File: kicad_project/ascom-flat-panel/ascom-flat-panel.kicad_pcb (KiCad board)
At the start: 2 copper layers, 12 parts, among them J1 Servo, J3 JST-XH LED, Q1 FQP30N06L, Q2 FQP30N06L, U1 XIAO-SAMD21-DIP

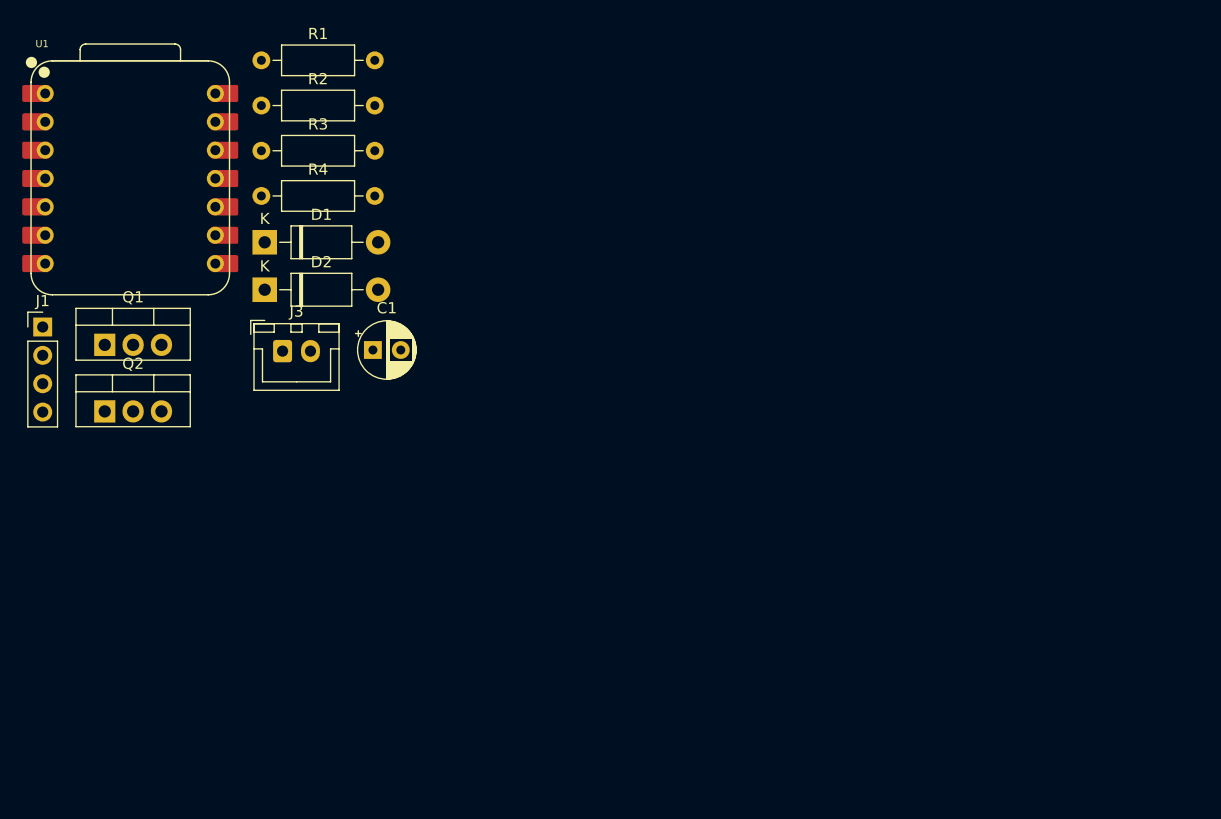
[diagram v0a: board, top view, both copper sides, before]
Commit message: Première mise en forme et routage du circuit - ajout modèle3D seeeduino
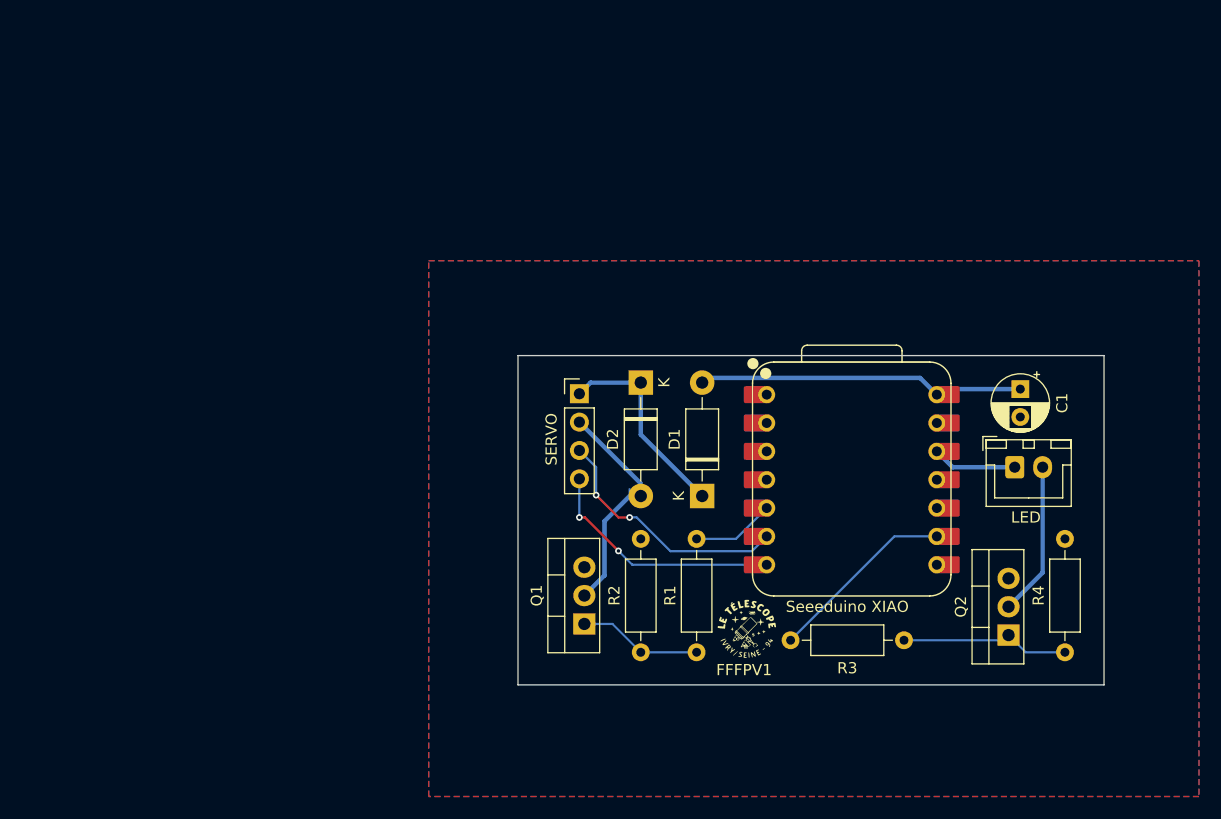
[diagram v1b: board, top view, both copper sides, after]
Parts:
- added G***: LOGO, LOGO, F.Cu at (118.5, 94.0)
- Seeeduino XIAO: renamed from U1
- moved Q2 83.4 mm to (141.9, 94.5), turned to 90 degrees
- moved R4 82.8 mm to (147.0, 96.1), turned to 90 degrees
- moved Seeeduino XIAO 70.0 mm to (128.0, 80.6)
- moved LED 66.4 mm to (142.5, 79.5)
- moved R1 65.8 mm to (114.0, 96.1), turned to 90 degrees
- moved R3 64.6 mm to (122.4, 95.0)
- moved R2 59.6 mm to (109.0, 96.1), turned to 90 degrees
- moved C1 58.1 mm to (143.0, 72.5), turned to -90 degrees
- moved Q1 49.7 mm to (103.9, 93.5), turned to 90 degrees
- moved SERVO 48.5 mm to (103.5, 72.9)
- moved D1 45.3 mm to (114.5, 82.1), turned to 90 degrees
- moved D2 34.7 mm to (109.0, 71.9), turned to -90 degrees
- renumbered J3 to LED, J1 to SERVO
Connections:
- Seeeduino XIAO pad 10: SERVO POSITION CONTROL -> unconnected-(U1-PA5_A9_D9_MISO-Pad10)
- Seeeduino XIAO pad 5: unconnected-(U1-PA8_A4_D4_SDA-Pad5) -> SERVO POWER CONTROL
- Seeeduino XIAO pad 6: unconnected-(U1-PA9_A5_D5_SCL-Pad6) -> SERVO POSITION CONTROL
- Seeeduino XIAO pad 8: SERVO POWER CONTROL -> unconnected-(U1-PB09_A7_D7_RX-Pad8)
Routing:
- net +5V: track 0.00 -> 29.5 mm
- net SERVO POSITION CONTROL: track 0.00 -> 22.5 mm, vias 0 -> 2
- net SERVO POSITION FEEDBACK: track 0.00 -> 22.0 mm, vias 0 -> 2
- net SERVO GND: track 0.00 -> 20.1 mm
- net SERVO VCC: track 0.00 -> 18.4 mm
- net LED_STRIP_POWER_CONTROL: track 0.00 -> 17.0 mm
- net Net-(Q2-G): track 0.00 -> 15.8 mm
- net Net-(J3-Pin_2): track 0.00 -> 13.8 mm
- net Net-(Q1-G): track 0.00 -> 11.1 mm
- net +3V3: track 0.00 -> 7.57 mm
- net SERVO POWER CONTROL: track 0.00 -> 7.42 mm
- added copper zone on B.Cu, net GND
- added copper zone on F.Cu, net GND
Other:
- board outline added: 52.5 x 29.5 mm
- board text added: "FFFPV1"

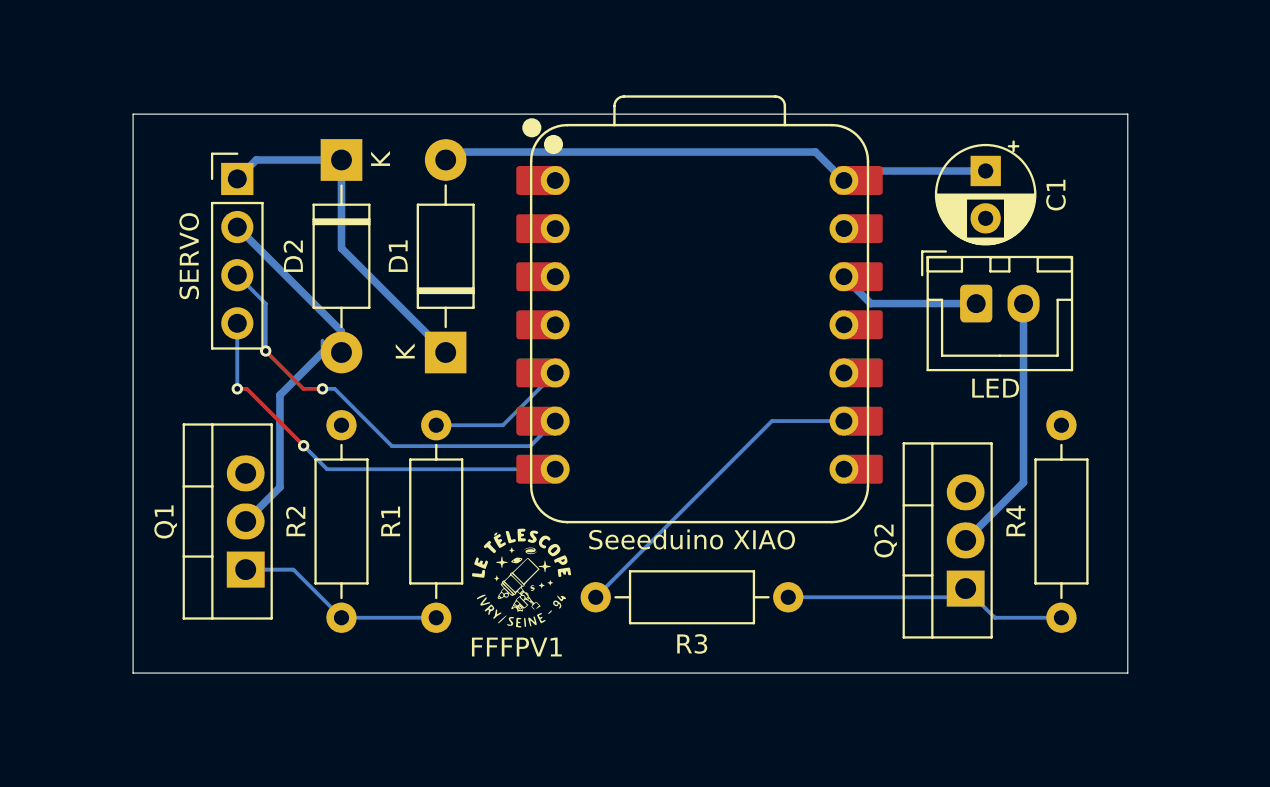
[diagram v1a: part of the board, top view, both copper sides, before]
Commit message: ajout perçage pour fixation + réajustement position logo club
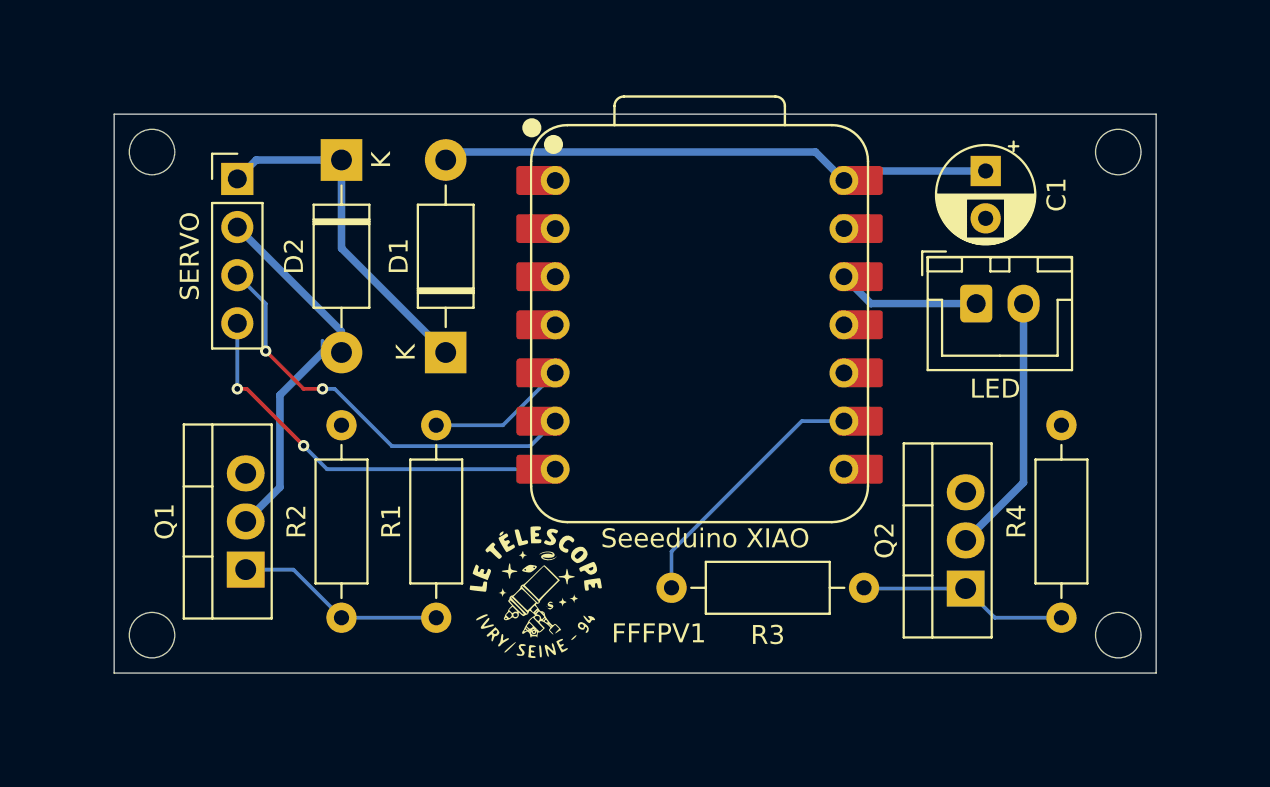
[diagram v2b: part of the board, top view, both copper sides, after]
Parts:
- moved R3 4.03 mm to (126.4, 94.5)
- moved G*** 1.06 mm to (119.2, 94.8)
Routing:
- net LED_STRIP_POWER_CONTROL: track 17.0 -> 13.9 mm
- net Net-(Q2-G): track 15.8 -> 13.0 mm
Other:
- board size 52.5 x 29.5 mm -> 55 x 29.5 mm

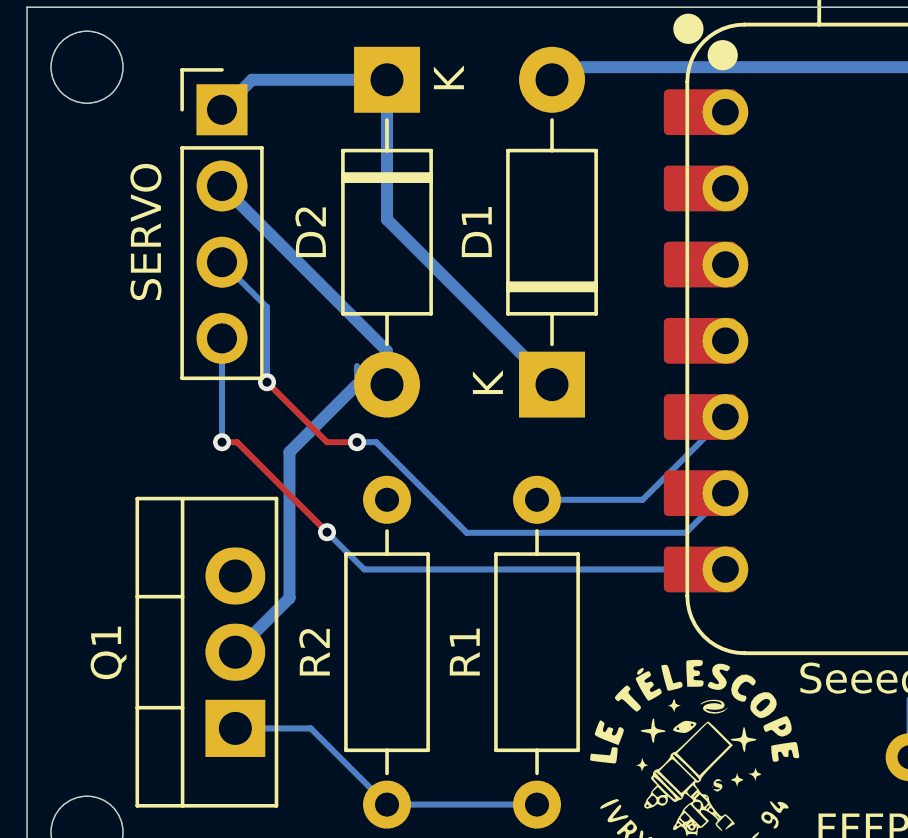
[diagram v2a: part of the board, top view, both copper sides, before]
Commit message: ajout des tolérances pcbway + quelques optimisations de routage (supression de vias)
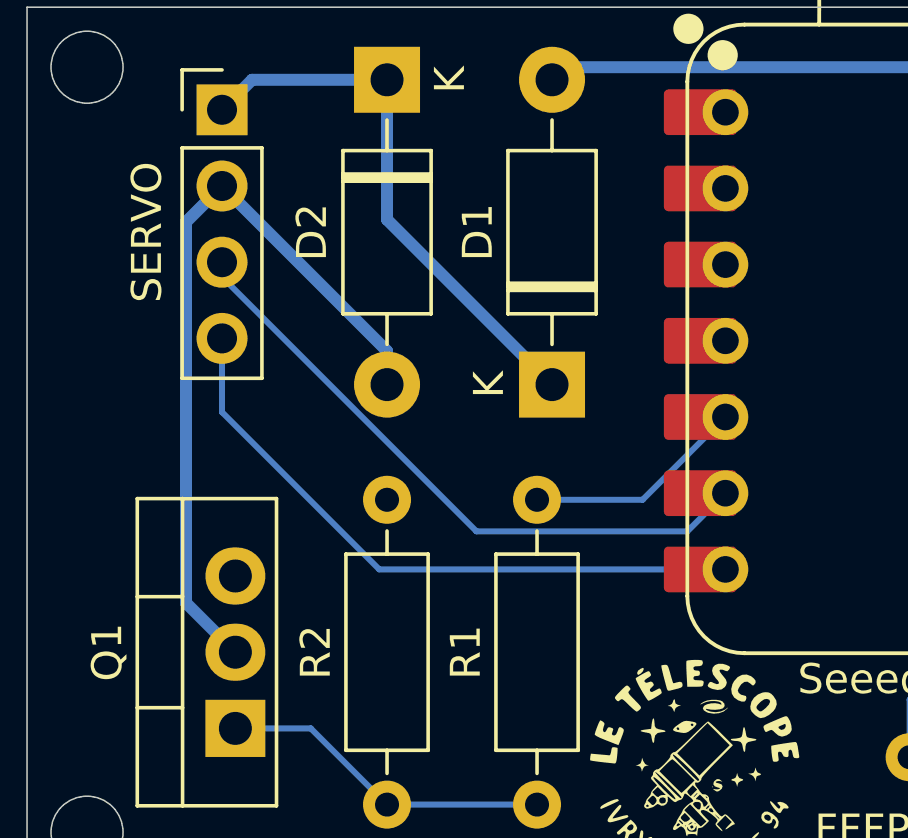
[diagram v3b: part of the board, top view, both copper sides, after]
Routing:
- net SERVO GND: track 20.1 -> 25.6 mm
- net SERVO POSITION CONTROL: track 22.5 -> 21.3 mm, vias 2 -> 0
- net SERVO POSITION FEEDBACK: track 22.0 -> 21.4 mm, vias 2 -> 0
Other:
- copper layers 2 -> 4
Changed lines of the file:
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@@
 	(generator_version "9.0")
 	(general
-		(thickness 1.6)
+		(thickness 1.600198)
 		(legacy_teardrops no)
 	)
@@
 	(layers
 		(0 "F.Cu" signal)
+		(4 "In1.Cu" signal)
+		(6 "In2.Cu" signal)
 		(2 "B.Cu" signal)
-		(9 "F.Adhes" user "F.Adhesive")
-		(11 "B.Adhes" user "B.Adhesive")
 		(13 "F.Paste" user)
 		(15 "B.Paste" user)
@@
 		(1 "F.Mask" user)
 		(3 "B.Mask" user)
-		(17 "Dwgs.User" user "User.Drawings")
-		(19 "Cmts.User" user "User.Comments")
-		(21 "Eco1.User" user "User.Eco1")
-		(23 "Eco2.User" user "User.Eco2")
 		(25 "Edge.Cuts" user)
 		(27 "Margin" user)
@@
 		(29 "B.CrtYd" user "B.Courtyard")
 		(35 "F.Fab" user)
-		(33 "B.Fab" user)
-		(39 "User.1" user)
-		(41 "User.2" user)
-		(43 "User.3" user)
-		(45 "User.4" user)
 	)
 	(setup
+		(stackup
+			(layer "F.SilkS"
+				(type "Top Silk Screen")
+			)
+			(layer "F.Paste"
+				(type "Top Solder Paste")
+			)
+			(layer "F.Mask"
+				(type "Top Solder Mask")
+				(thickness 0.01)
+			)
+			(layer "F.Cu"
+				(type "copper")
+				(thickness 0.035)
+			)
+			(layer "dielectric 1"
+				(type "core")
+				(thickness 0.480066)
+				(material "FR4")
+				(epsilon_r 4.5)
+				(loss_tangent 0.02)
+			)
+			(layer "In1.Cu"
+				(type "copper")
+				(thickness 0.035)
+			)
+			(layer "dielectric 2"
+				(type "prepreg")
+				(thickness 0.480066)
+				(material "FR4")
+				(epsilon_r 4.5)
+				(loss_tangent 0.02)
+			)
+			(layer "In2.Cu"
+				(type "copper")
+				(thickness 0.035)
+			)
+			(layer "dielectric 3"
+				(type "core")
+				(thickness 0.480066)
+				(material "FR4")
+				(epsilon_r 4.5)
+				(loss_tangent 0.02)
+			)
+			(layer "B.Cu"
+				(type "copper")
+				(thickness 0.035)
+			)
+			(layer "B.Mask"
+				(type "Bottom Solder Mask")
+				(thickness 0.01)
+			)
+			(layer "B.Paste"
+				(type "Bottom Solder Paste")
+			)
+			(layer "B.SilkS"
+				(type "Bottom Silk Screen")
+			)
+			(copper_finish "None")
+			(dielectric_constraints no)
+		)
 		(pad_to_mask_clearance 0)
+		(solder_mask_min_width 0.1016)
 		(allow_soldermask_bridges_in_footprints no)
 		(tenting front back)
@@
 	)
 	(segment
-		(start 105.75 89.195)
-		(end 103.945 91)
+		(start 102.299 76.661)
+		(end 103.5 75.46)
 		(width 0.4)
 		(layer "B.Cu")
@@
 	)
 	(segment
-		(start 109 82.08)
-		(end 109 80.96)
-		(width 0.2)
-		(layer "B.Cu")
-		(net 4)
-	)
-	(segment
-		(start 108 82.08)
-		(end 108 81.46)
-		(width 0.2)
-		(layer "B.Cu")
-		(net 4)
-	)
-	(segment
-		(start 105.75 84.33)
-		(end 105.75 89.195)
+		(start 103.945 91)
+		(end 102.299 89.354)
 		(width 0.4)
 		(layer "B.Cu")
@@
 	)
 	(segment
-		(start 108 82.08)
-		(end 105.75 84.33)
+		(start 109 82.08)
+		(end 109 80.96)
 		(width 0.4)
 		(layer "B.Cu")
@@
 	)
 	(segment
-		(start 104 84)
-		(end 107 87)
-		(width 0.2)
-		(layer "F.Cu")
-		(net 5)
-	)
-	(segment
-		(start 103.5 84)
-		(end 104 84)
-		(width 0.2)
-		(layer "F.Cu")
-		(net 5)
-	)
-	(via
-		(at 107 87)
-		(size 0.6)
-		(drill 0.3)
-		(layers "F.Cu" "B.Cu")
-		(net 5)
-	)
-	(via
-		(at 103.5 84)
-		(size 0.6)
-		(drill 0.3)
-		(layers "F.Cu" "B.Cu")
-		(net 5)
-	)
-	(segment
-		(start 108.24 88.24)
-		(end 120.28 88.24)
-		(width 0.2)
+		(start 102.299 89.354)
+		(end 102.299 76.661)
+		(width 0.4)
 		(layer "B.Cu")
-		(net 5)
+		(net 4)
 	)
 	(segment
-		(start 107 87)
-		(end 108.24 88.24)
+		(start 120.28 88.24)
+		(end 108.74 88.24)
 		(width 0.2)
 		(layer "B.Cu")
@@
 	)
 	(segment
-		(start 103.5 80.54)
-		(end 103.5 84)
+		(start 103.5 83)
+		(end 103.5 80.54)
 		(width 0.2)
 		(layer "B.Cu")
@@
 	)
 	(segment
-		(start 108 84)
-		(end 107 84)
-		(width 0.2)
-		(layer "F.Cu")
-		(net 6)
-	)
-	(segment
-		(start 107 84)
-		(end 105 82)
-		(width 0.2)
-		(layer "F.Cu")
-		(net 6)
-	)
-	(via
-		(at 108 84)
-		(size 0.6)
-		(drill 0.3)
-		(layers "F.Cu" "B.Cu")
-		(net 6)
-	)
-	(via
-		(at 105 82)
-		(size 0.6)
-		(drill 0.3)
-		(layers "F.Cu" "B.Cu")
-		(net 6)
-	)
-	(segment
-		(start 111.65805 87.021)
-		(end 108.63705 84)
+		(start 108.74 88.24)
+		(end 103.5 83)
 		(width 0.2)
 		(layer "B.Cu")
-		(net 6)
+		(net 5)
 	)
 	(segment
-		(start 103.5 78)
-		(end 105 79.5)
+		(start 103.5 78.490603)
+		(end 103.5 78)
 		(width 0.2)
 		(layer "B.Cu")
@@
 	)
 	(segment
-		(start 118.959 87.021)
-		(end 111.65805 87.021)
+		(start 111.980397 86.971)
+		(end 103.5 78.490603)
 		(width 0.2)
 		(layer "B.Cu")
@@
 	)
 	(segment
-		(start 108.63705 84)
-		(end 108 84)
+		(start 119.009 86.971)
+		(end 111.980397 86.971)
 		(width 0.2)
 		(layer "B.Cu")
@@
 	(segment
 		(start 120.28 85.7)
-		(end 118.959 87.021)
-		(width 0.2)
-		(layer "B.Cu")
-		(net 6)
-	)
-	(segment
-		(start 105 79.5)
-		(end 105 82)
+		(end 119.009 86.971)
 		(width 0.2)
 		(layer "B.Cu")
